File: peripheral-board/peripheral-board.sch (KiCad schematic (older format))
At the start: 7 parts, among them CON1001 AVR-ISP-10, IC1001 ATTINY48-A, P1001 Peripheral Bus, P1002 Power

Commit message: added some audio circuitry
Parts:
- added D1001: Status LED, symbol LED_RABG
- added SW1001: Power, lib:SMD-TACT-5.2x5.2x2mm, symbol SW_PUSH
- R1001, R1002: footprint (none) -> Resistors_SMD:R_0805
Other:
- moved on the sheet: P1001, P1002, R1001, R1002

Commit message: added battery charger schematic
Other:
- note added: "status led on sd card slave select?"
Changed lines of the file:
@@
 LIBS:joystick
 LIBS:digital-pot
+LIBS:vref
 LIBS:peripheral-board-cache
 EELAYER 26 0
@@
 $Descr A4 11693 8268
 encoding utf-8
-Sheet 1 9
+Sheet 1 10
 Title ""
 Date ""
@@
 	0    -1   -1   0
 $EndComp
+Text Notes 2800 800  0    60   ~ 0
+status led on sd card slave select?
 $EndSCHEMATC

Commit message: added audio jack
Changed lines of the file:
@@
 $EndSheet
 $Sheet
-S 6650 3100 650  300
+S 7300 5000 700  300
 U 5819E78C
 F0 "Mouse" 60
 F1 "mouse.sch" 60
-F2 "X" O L 6650 3200 60
-F3 "Y" O L 6650 3300 60
+F2 "X" O L 7300 5100 60
+F3 "Y" O L 7300 5200 60
 $EndSheet
 $Comp
@@
 F0 "Power Supply" 60
 F1 "power.sch" 60
-F2 "~SHDN" I L 9100 2700 60
+F2 "SHDN" I L 9100 2650 60
 $EndSheet
 $Sheet

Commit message: audio circuitry
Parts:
- RP1001: symbol R_PACK4 -> R_Pack04
- SW1001: symbol SW_PUSH -> SW_Push
- U1001: renamed from IC1001; symbol ATTINY48-A -> ATTINY48-AU
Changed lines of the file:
@@
 EESchema Schematic File Version 2
+LIBS:peripheral-board-rescue
 LIBS:power
 LIBS:device
@@
 LIBS:digital-pot
 LIBS:vref
+LIBS:switches
 LIBS:peripheral-board-cache
 EELAYER 26 0
@@
 $EndSheet
 $Comp
-L ATTINY48-A IC1001
+L ATTINY48-AU U1001
 U 1 1 5819EBDE
 P 4000 4200
-F 0 "IC1001" H 3400 4250 50  0000 C CNN
+F 0 "U1001" H 3400 4250 50  0000 C CNN
 F 1 "ATTINY48-A" H 3450 4150 50  0000 C CNN
 F 2 "Housings_QFP:TQFP-32_7x7mm_Pitch0.8mm" H 4000 5775 50  0001 C CIN
@@
 SPI_SCK
 $Comp
-L GND #PWR01
+L GND #PWR1013
 U 1 1 581F4F29
 P 5150 6850
-F 0 "#PWR01" H 5150 6600 50  0001 C CNN
+F 0 "#PWR1013" H 5150 6600 50  0001 C CNN
 F 1 "GND" H 5155 6677 50  0000 C CNN
 F 2 "" H 5150 6850 50  0000 C CNN
@@
 NoConn ~ 4550 6500
 $Comp
-L GND #PWR02
+L GND #PWR1010
 U 1 1 581F524B
 P 3000 5700
-F 0 "#PWR02" H 3000 5450 50  0001 C CNN
+F 0 "#PWR1010" H 3000 5450 50  0001 C CNN
 F 1 "GND" H 3005 5527 50  0000 C CNN
 F 2 "" H 3000 5700 50  0000 C CNN
@@
 CLK33
 $Comp
-L GND #PWR03
+L GND #PWR1001
 U 1 1 581F752E
 P 1000 1950
-F 0 "#PWR03" H 1000 1700 50  0001 C CNN
+F 0 "#PWR1001" H 1000 1700 50  0001 C CNN
 F 1 "GND" V 1005 1822 50  0000 R CNN
 F 2 "" H 1000 1950 50  0000 C CNN
@@
 $EndComp
 $Comp
-L GND #PWR04
+L GND #PWR1002
 U 1 1 581F7634
 P 1000 2800
-F 0 "#PWR04" H 1000 2550 50  0001 C CNN
+F 0 "#PWR1002" H 1000 2550 50  0001 C CNN
 F 1 "GND" V 1005 2672 50  0000 R CNN
 F 2 "" H 1000 2800 50  0000 C CNN
@@
 $EndComp
 $Comp
-L GND #PWR05
+L GND #PWR1003
 U 1 1 581F76B8
 P 1000 3200
-F 0 "#PWR05" H 1000 2950 50  0001 C CNN
+F 0 "#PWR1003" H 1000 2950 50  0001 C CNN
 F 1 "GND" V 1005 3072 50  0000 R CNN
 F 2 "" H 1000 3200 50  0000 C CNN
@@
 $EndComp
 $Comp
-L GND #PWR06
+L GND #PWR1004
 U 1 1 581F7709
 P 1000 3500
-F 0 "#PWR06" H 1000 3250 50  0001 C CNN
+F 0 "#PWR1004" H 1000 3250 50  0001 C CNN
 F 1 "GND" V 1005 3372 50  0000 R CNN
 F 2 "" H 1000 3500 50  0000 C CNN
@@
 $EndComp
 $Comp
-L GND #PWR07
+L GND #PWR1005
 U 1 1 581F7744
 P 1000 4200
-F 0 "#PWR07" H 1000 3950 50  0001 C CNN
+F 0 "#PWR1005" H 1000 3950 50  0001 C CNN
 F 1 "GND" V 1005 4072 50  0000 R CNN
 F 2 "" H 1000 4200 50  0000 C CNN
@@
 $EndComp
 $Comp
-L GND #PWR08
+L GND #PWR1006
 U 1 1 581F77D7
 P 1000 4450
-F 0 "#PWR08" H 1000 4200 50  0001 C CNN
+F 0 "#PWR1006" H 1000 4200 50  0001 C CNN
 F 1 "GND" V 1005 4322 50  0000 R CNN
 F 2 "" H 1000 4450 50  0000 C CNN
@@
 $EndComp
 $Comp
-L GND #PWR09
+L GND #PWR1008
 U 1 1 581F7812
 P 1000 4950
-F 0 "#PWR09" H 1000 4700 50  0001 C CNN
+F 0 "#PWR1008" H 1000 4700 50  0001 C CNN
 F 1 "GND" V 1005 4822 50  0000 R CNN
 F 2 "" H 1000 4950 50  0000 C CNN
@@
 $EndComp
 $Comp
-L +24V #PWR010
+L +24V #PWR1007
 U 1 1 581F7F97
 P 1000 4800
-F 0 "#PWR010" H 1000 4650 50  0001 C CNN
+F 0 "#PWR1007" H 1000 4650 50  0001 C CNN
 F 1 "+24V" V 1000 4950 50  0000 L CNN
 F 2 "" H 1000 4800 50  0000 C CNN
@@
 $EndComp
 $Comp
-L +3V3 #PWR011
+L +3V3 #PWR1009
 U 1 1 581F7FED
 P 1000 5100
-F 0 "#PWR011" H 1000 4950 50  0001 C CNN
+F 0 "#PWR1009" H 1000 4950 50  0001 C CNN
 F 1 "+3V3" V 1000 5250 50  0000 L CNN
 F 2 "" H 1000 5100 50  0000 C CNN
@@
 $EndSheet
 $Comp
-L R_PACK4 RP1001
+L R_Pack04 RP1001
 U 1 1 581F7416
-P 2950 6850
-F 0 "RP1001" H 2950 7415 50  0000 C CNN
-F 1 "10k" H 2950 7324 50  0000 C CNN
-F 2 "Resistors_SMD:R_Cat16-4" H 2950 6850 50  0001 C CNN
-F 3 "" H 2950 6850 50  0000 C CNN
-	1    2950 6850
-	1    0    0    -1
+P 2950 6700
+F 0 "RP1001" V 3150 6700 50  0000 C CNN
+F 1 "10k" V 2650 6700 50  0000 C CNN
+F 2 "Resistors_SMD:R_Cat16-4" H 2950 6700 50  0001 C CNN
+F 3 "" H 2950 6700 50  0000 C CNN
+	1    2950 6700
+	0    1    1    0
 $EndComp
 Wire Wire Line
@@
 	3150 6900 3150 6800
 $Comp
-L GND #PWR012
+L GND #PWR1012
 U 1 1 581F76DB
 P 2700 6850
-F 0 "#PWR012" H 2700 6600 50  0001 C CNN
+F 0 "#PWR1012" H 2700 6600 50  0001 C CNN
 F 1 "GND" H 2705 6677 50  0000 C CNN
 F 2 "" H 2700 6850 50  0000 C CNN
@@
 Connection ~ 2700 6500
 $Comp
-L +3V3 #PWR013
+L +3V3 #PWR1011
 U 1 1 581F7984
 P 2700 6400
-F 0 "#PWR013" H 2700 6250 50  0001 C CNN
+F 0 "#PWR1011" H 2700 6250 50  0001 C CNN
 F 1 "+3V3" H 2715 6573 50  0000 C CNN
 F 2 "" H 2700 6400 50  0000 C CNN
@@
 $EndComp
 $Comp
-L SW_PUSH SW1001
+L SW_Push SW1001
 U 1 1 5823964C
 P 2500 1300

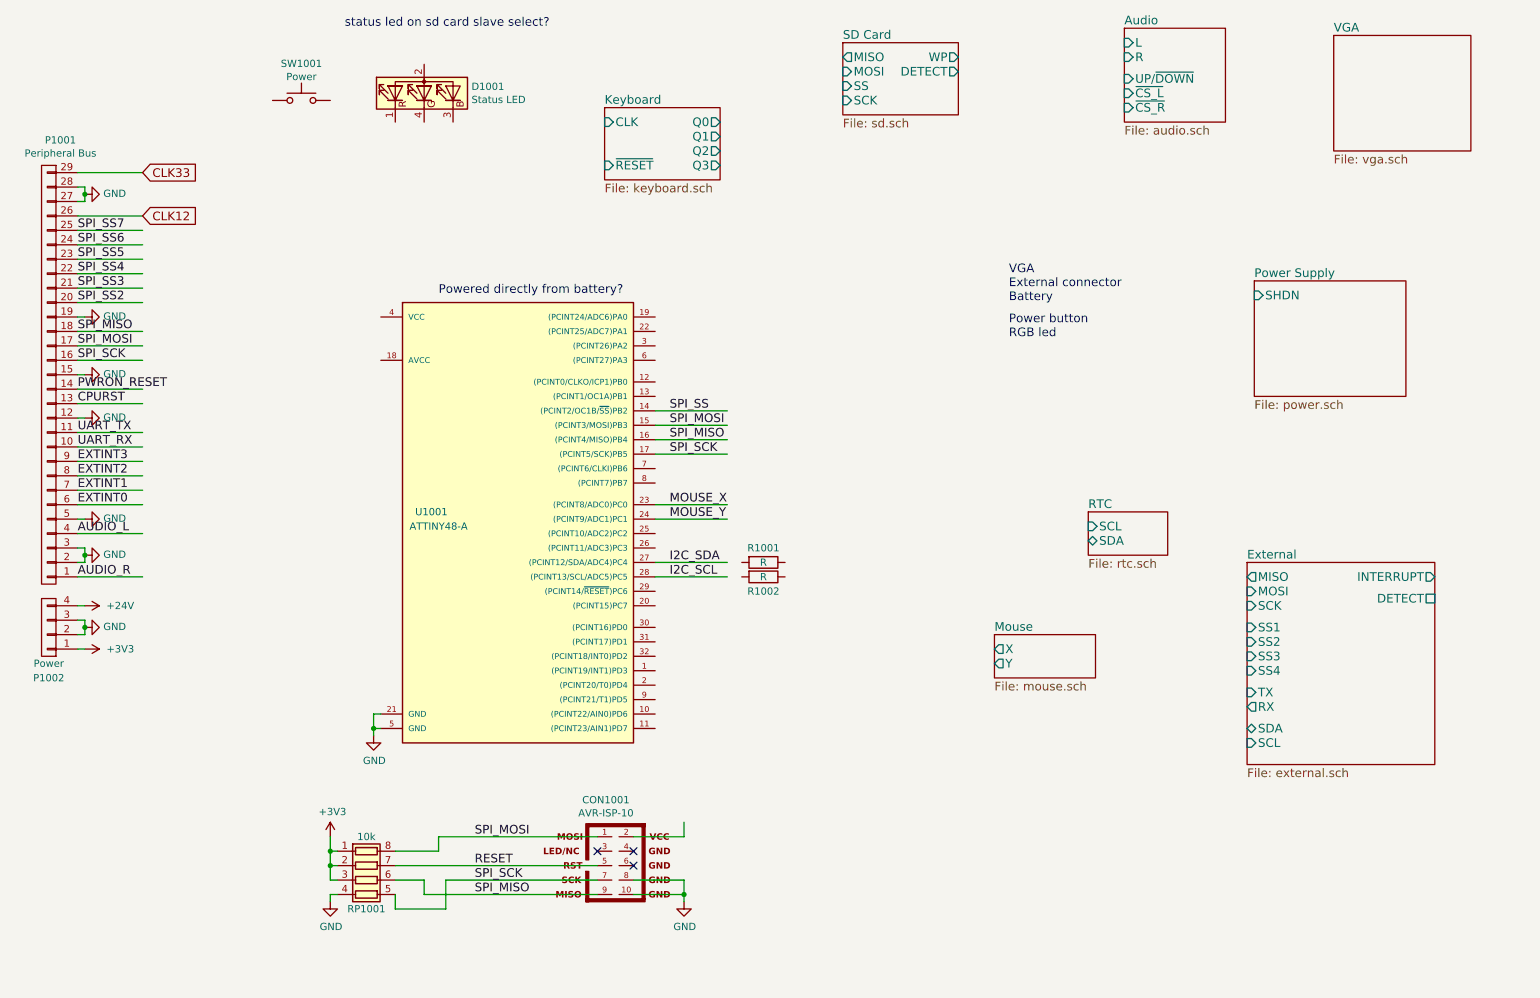
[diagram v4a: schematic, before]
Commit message: power supply component placement
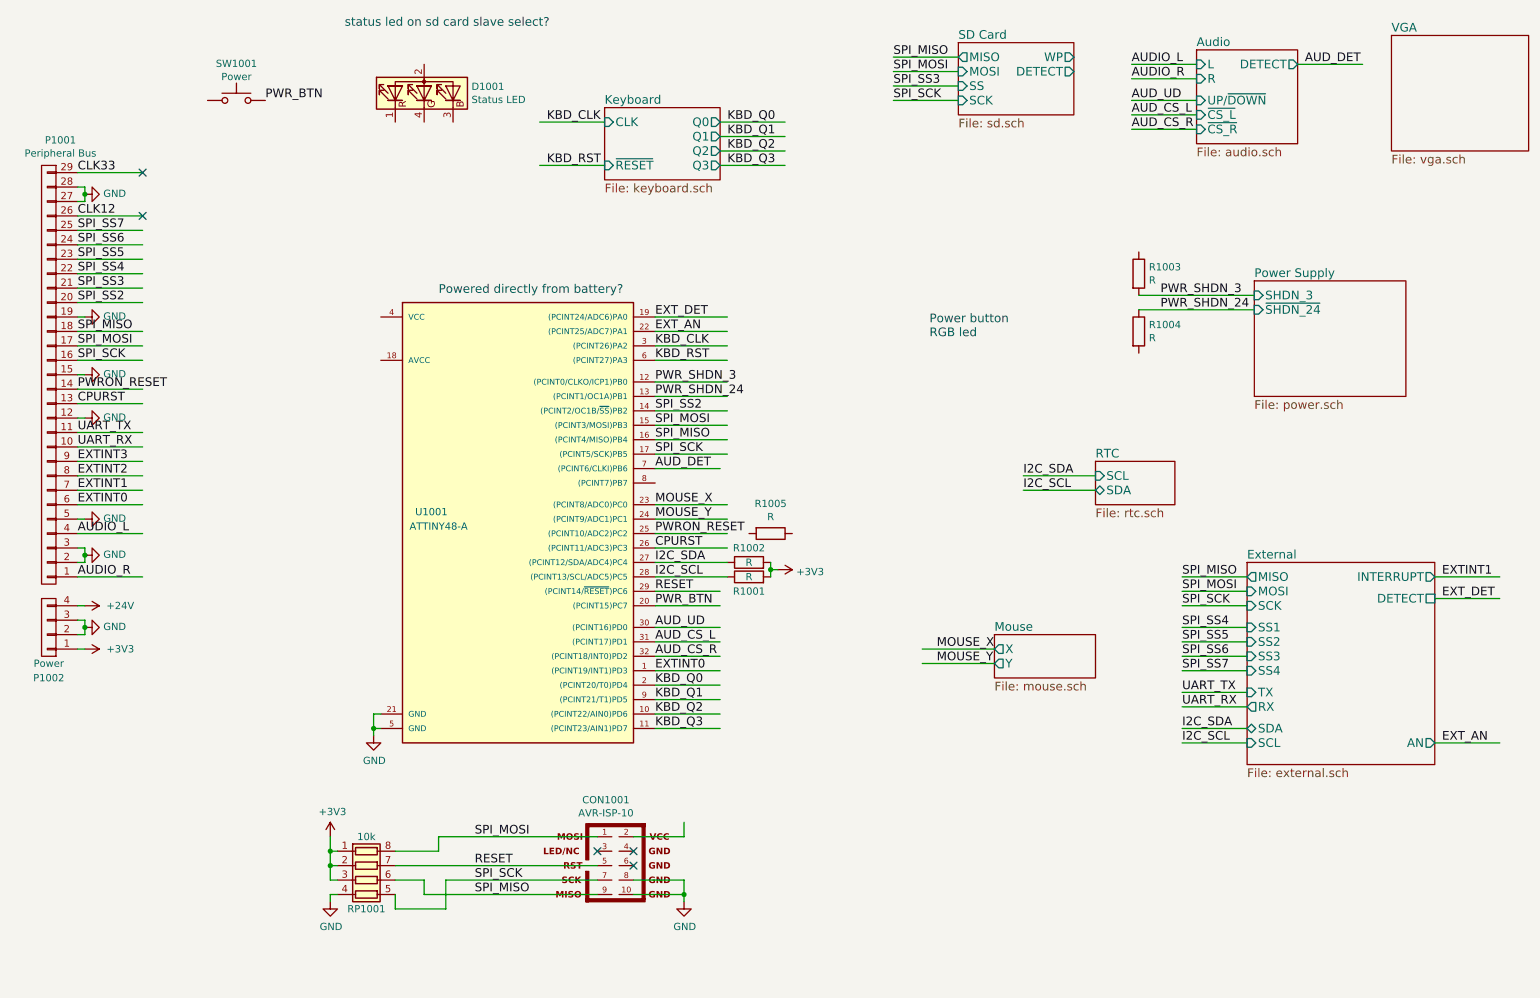
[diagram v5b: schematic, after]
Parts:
- added R1003, R1004, R1005: R, Resistors_SMD:R_0805, symbol R
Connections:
- net labels added: AUD_CS_L, AUD_CS_R, AUD_DET, AUD_UD, EXT_AN, EXT_DET, KBD_CLK, KBD_Q0, KBD_Q1, KBD_Q2, KBD_Q3, KBD_RST, PWR_BTN, PWR_SHDN_24, PWR_SHDN_3
- net labels removed: SPI_SS
- wire segments 69 -> 126
- no-connect marks 3 -> 5
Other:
- note removed: "VGA\nExternal connector\nBattery"
- moved on the sheet: R1001, R1002, SW1001
